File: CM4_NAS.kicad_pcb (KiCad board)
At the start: 4 copper layers, 88.5 x 72.5 mm, 32 parts, among them J1 USB_A, J10 Conn_02x07_Odd_Even, J11 Conn_01x03, J12 Conn_01x03, J13 Conn_02x06_Odd_Even, J15 Temp_Sensor, J2 HDMI_header, J3 PCIe_conn, J4 Sata_PWR, J5 PWR_IN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

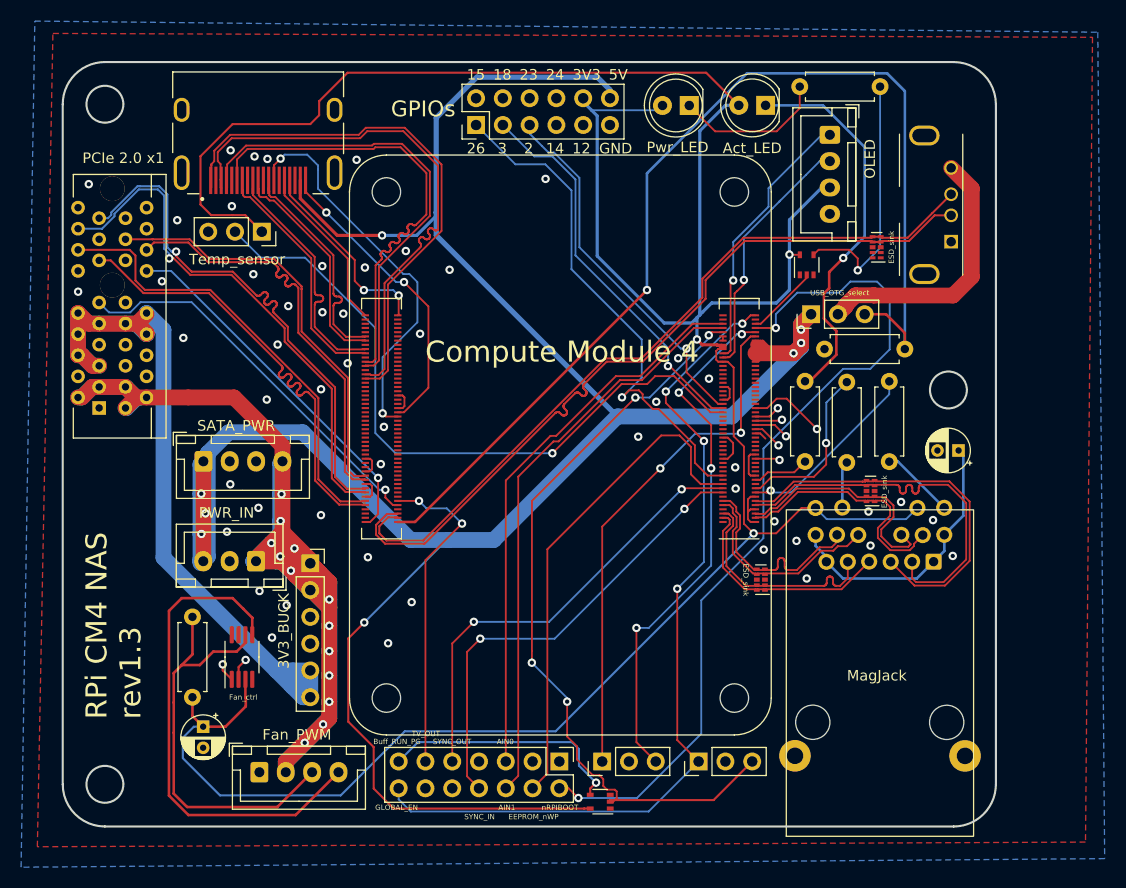
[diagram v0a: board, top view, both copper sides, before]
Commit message: rev1.4 Add pin to OLED connector for button, use SMD caps and LEDs, more info on silkscreen and fixed some traces.
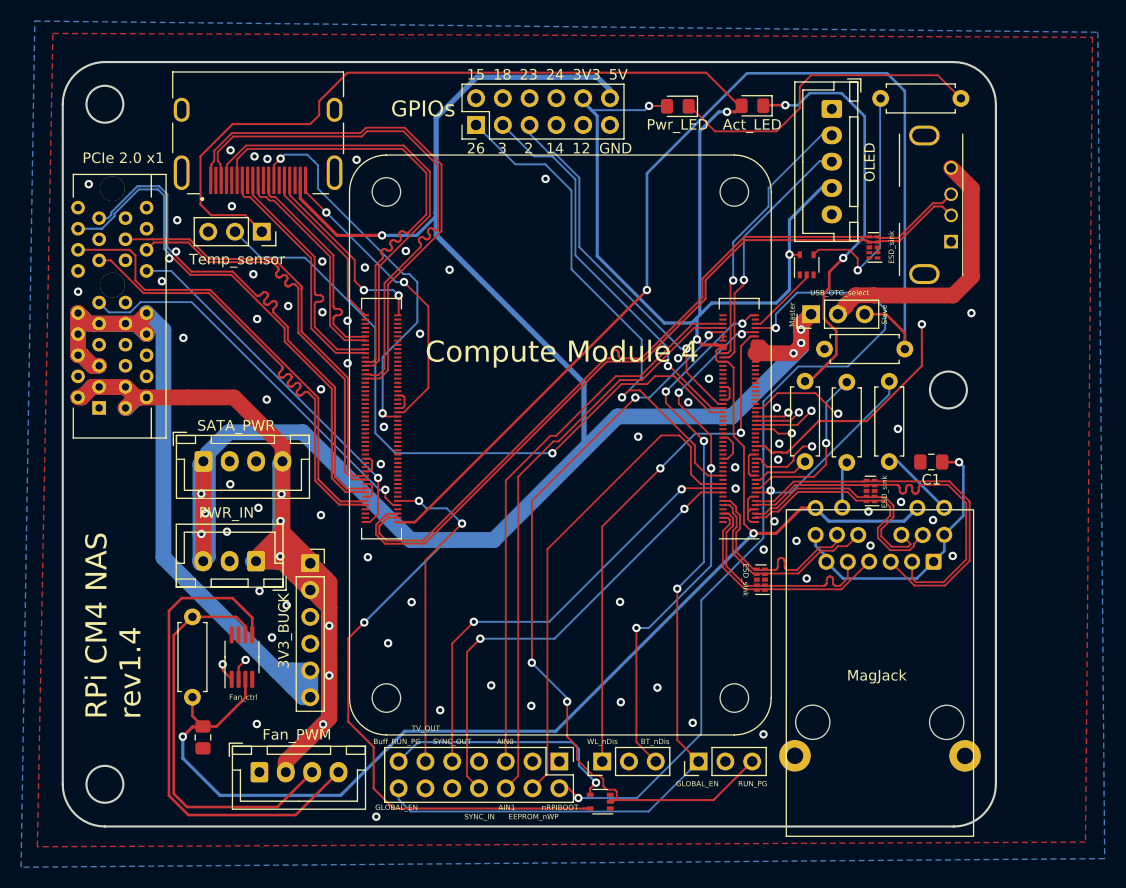
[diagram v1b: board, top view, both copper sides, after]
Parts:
- C1, C2: footprint Capacitor_THT:CP_Radial_D4.0mm_P2.00mm -> Capacitor_SMD:C_0805_2012Metric_Pad1.18x1.45mm_HandSolder
- D1, D2: footprint LED_THT:LED_D5.0mm -> LED_SMD:LED_0805_2012Metric_Pad1.15x1.40mm_HandSolder
- J8: footprint Connector_JST:JST_XH_B4B-XH-A_1x04_P2.50mm_Vertical -> Connector_JST:JST_XH_B5B-XH-A_1x05_P2.50mm_Vertical
- R5: value 36K -> 36K 1%
- moved R6 15.3 mm to (175.2, 72.8), turned to 180 degrees
- moved C1 2.81 mm to (172.4, 107.2)
- moved J8 2.46 mm to (163.0, 73.8)
- moved D1 1.24 mm to (155.5, 73.4)
- moved D2 1.08 mm to (148.4, 73.5)
- moved C2 1.02 mm to (103.4, 133.4)
- moved U5 0.31 mm to (166.9, 86.9)
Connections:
- J8 pad 1: /SDA -> /OLED_BTN
- J8 pad 2: /SCL -> /SDA
- J8 pad 3: /+3.3v -> /SCL
- J8 pad 4: GND -> /+3.3v
- Module1 pad 37: /GPIO7 -> /OLED_BTN
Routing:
- net /OLED_BTN: track 0.00 -> 47.4 mm, vias 0 -> 1
- net Net-(D2-Pad1): track 14.5 -> 31.1 mm
- net Net-(D1-Pad1): track 36.8 -> 39.8 mm, vias 1 -> 2
- net +5V: track 235.8 -> 237.7 mm
- net /GPIO15: track 55.4 -> 57.1 mm
- net /GPIO18: track 53.5 -> 55.0 mm
- net /USB2_P: track 74.6 -> 73.1 mm
- net Net-(J7-Pad3): track 40.2 -> 38.7 mm
- net GND: track 21.0 -> 19.8 mm, vias 51 -> 66
- net Net-(R6-Pad2): track 24.2 -> 23.1 mm
- net /USB2_N: track 72.0 -> 73.1 mm
- net /nRPIBOOT: track 82.8 -> 81.8 mm
- net /GPIO24: track 64.8 -> 63.8 mm
- net /GPIO12: track 62.5 -> 63.4 mm
- net /GPIO14: track 64.1 -> 63.3 mm
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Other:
- board text added: "BT_nDis"
- board text added: "Master"
- board text added: "RPi CM4 NAS rev1.4"
- board text added: "RUN_PG"
- board text added: "Slave"
- board text added: "WL_nDis"
- board text removed: "RPi CM4 NAS rev1.3"
